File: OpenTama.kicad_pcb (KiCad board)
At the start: 2 copper layers, 45 x 58.2 mm, 65 parts, among them J1 Conn_01x09, J2 Conn_01x14, J3 Conn_01x07, J4 USB_C_Receptacle_USB2.0, J5 Conn_01x14, Q1 BSS138, Q2 BSS138, Q3 BSS84, SW1 LEFT, SW2 MIDDLE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

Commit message: PCB Trace, Via, Zone Reset
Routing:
- net +3V3: track 217.2 -> 0.00 mm, vias 7 -> 0
- net +BATT: track 108.7 -> 0.00 mm, vias 4 -> 0
- net +5V: track 106.7 -> 0.00 mm, vias 2 -> 0
- net -BATT: track 95.5 -> 0.00 mm, vias 69 -> 0
- net USB_D+: track 51.2 -> 0.00 mm
- net VBATT_MEAS: track 49.9 -> 0.00 mm, vias 2 -> 0
- net LEFT_BTN: track 48.3 -> 0.00 mm
- net USB_D-: track 47.9 -> 0.00 mm
- net I2C1_SCL: track 47.2 -> 0.00 mm
- net I2C1_SDA: track 45.0 -> 0.00 mm
- net NCHARG: track 42.5 -> 0.00 mm, vias 2 -> 0
- net VBATT_ANA: track 39.4 -> 0.00 mm, vias 4 -> 0
- net USART1_RX: track 38.0 -> 0.00 mm, vias 2 -> 0
- net Net-(J2-Pin_1): track 34.0 -> 0.00 mm
- net RIGHT_BTN: track 31.9 -> 0.00 mm
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- removed copper zone on B.Cu, net -BATT
- removed copper zone on F.Cu, net -BATT

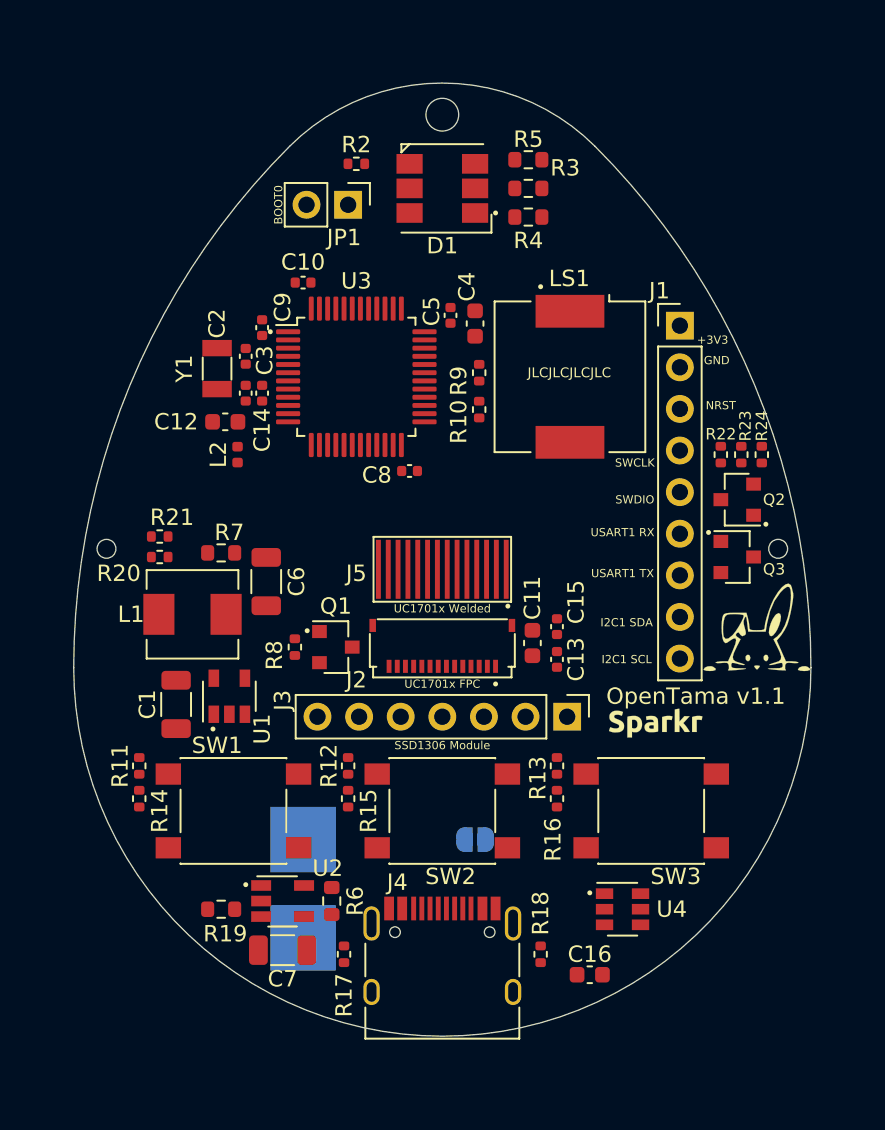
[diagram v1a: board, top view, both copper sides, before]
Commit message: Converted to 1206
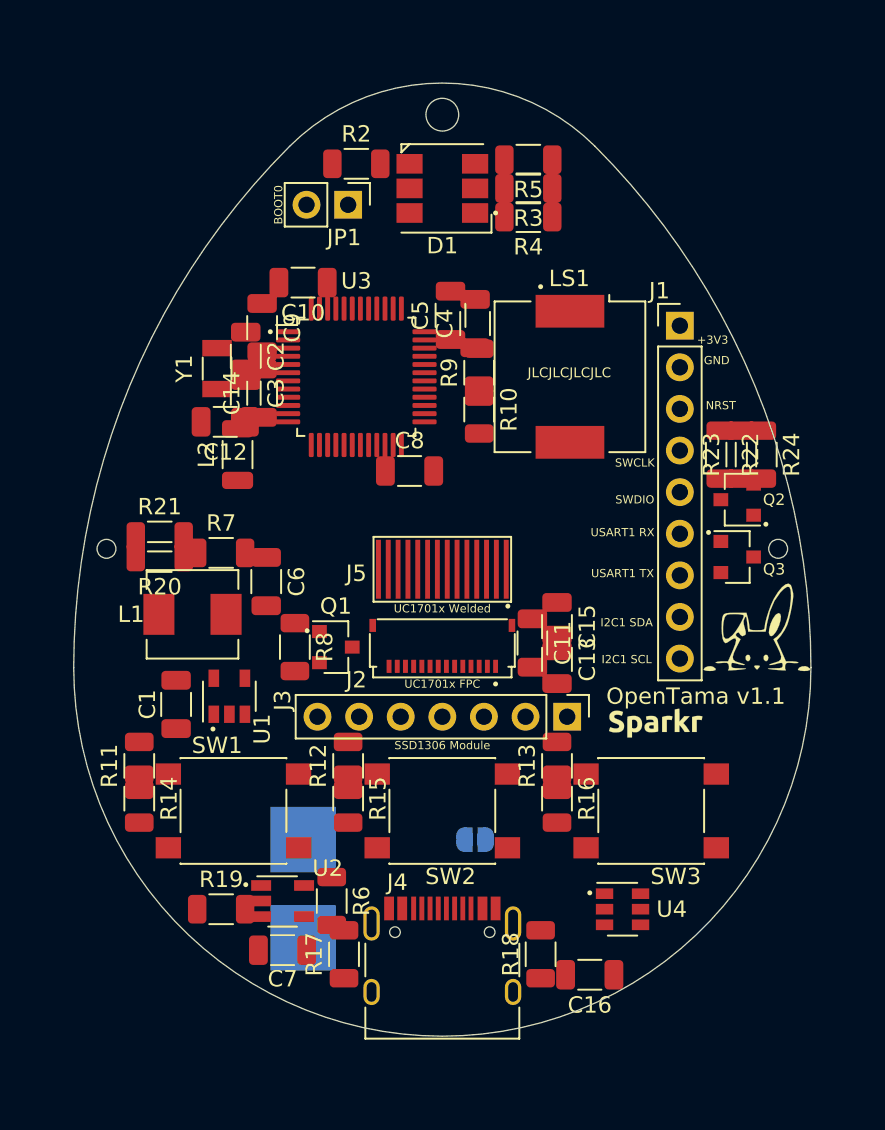
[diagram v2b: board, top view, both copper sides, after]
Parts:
- C10, C13, C14, C15, C2, C3, C5, C8, C9: footprint Capacitor_SMD:C_0402_1005Metric -> Capacitor_SMD:C_1206_3216Metric
- C11, C12, C16, C4: footprint Capacitor_SMD:C_0603_1608Metric -> Capacitor_SMD:C_1206_3216Metric
- L2: footprint Inductor_SMD:L_0402_1005Metric -> Inductor_SMD:L_1206_3216Metric
- R10, R11, R12, R13, R14, R15, R16, R17, R18, R2, R20, R21, R22, R23, R24, R8, R9: footprint Resistor_SMD:R_0402_1005Metric -> Resistor_SMD:R_1206_3216Metric
- R19, R3, R4, R5, R6, R7: footprint Resistor_SMD:R_0603_1608Metric -> Resistor_SMD:R_1206_3216Metric
